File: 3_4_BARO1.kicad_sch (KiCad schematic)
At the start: 4 parts, among them U901 LPS22HH

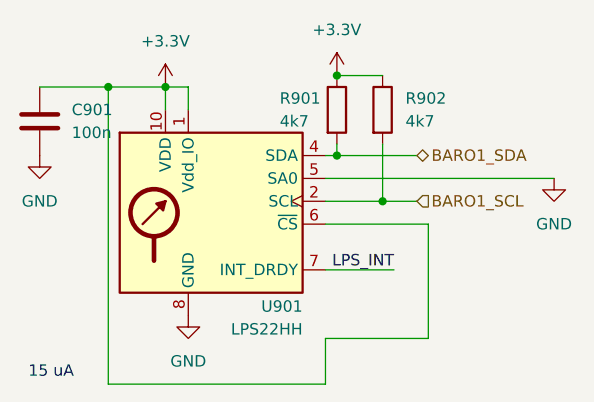
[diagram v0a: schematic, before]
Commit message: Finished restructuring schematic
Most components that were on page 3 are now in their own page
Added high-frequency 4.7 uF capacitor to servo power line
Continuity sensing on pyrochannels is multiplexed to one ADC on NAV.
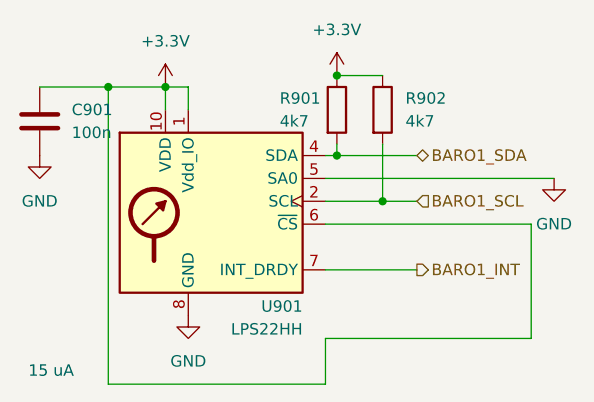
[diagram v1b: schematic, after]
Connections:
- net LPS_INT renamed BARO1_INT
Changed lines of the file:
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@@
-	(wire
-		(pts
-			(xy 152.4 105.41) (xy 160.02 105.41)
-		)
-		(stroke
-			(width 0)
-			(type default)
-		)
-	)
 	(wire
 		(pts
@@
 	(wire
 		(pts
-			(xy 163.83 100.33) (xy 163.83 113.03)
+			(xy 175.26 100.33) (xy 175.26 113.03)
 		)
 		(stroke
@@
 	(wire
 		(pts
+			(xy 152.4 105.41) (xy 162.56 105.41)
+		)
+		(stroke
+			(width 0)
+			(type default)
+		)
+	)
+	(wire
+		(pts
 			(xy 128.27 85.09) (xy 134.62 85.09)
 		)
@@
 	(wire
 		(pts
-			(xy 152.4 100.33) (xy 163.83 100.33)
+			(xy 152.4 100.33) (xy 175.26 100.33)
 		)
 		(stroke
@@
 	(wire
 		(pts
-			(xy 163.83 113.03) (xy 152.4 113.03)
+			(xy 152.4 113.03) (xy 175.26 113.03)
 		)
 		(stroke
@@
 		)
 	)
-	(label "LPS_INT"
-		(at 160.02 105.41 180)
-		(effects
-			(font
-				(size 1.27 1.27)
-			)
-			(justify right bottom)
-		)
-	)
 	(hierarchical_label "BARO1_SCL"
 		(shape input)
@@
 		(effects
 			(font
+				(size 1.27 1.27)
+			)
+			(justify left)
+		)
+	)
+	(hierarchical_label "BARO1_INT"
+		(shape output)
+		(at 162.56 105.41 0)
+		(effects
+			(font
